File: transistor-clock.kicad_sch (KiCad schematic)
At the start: 48 parts, among them J1 Screw_Terminal_01x02, J10 m0_return, J11 m1_return, J12 h0_return, J13 h1_return, J8 s0_return, J9 s1_return, Q1 MMBT3904, Q2 MMBT3904, Q3 DMP3099L, Q4 2N7002, Q5 MMBT3904, Q6 MMBT3904, Q7 MMBT3904, Q8 MMBT3904, T1 Transformer_1P_SS, T2 CL2-20-12

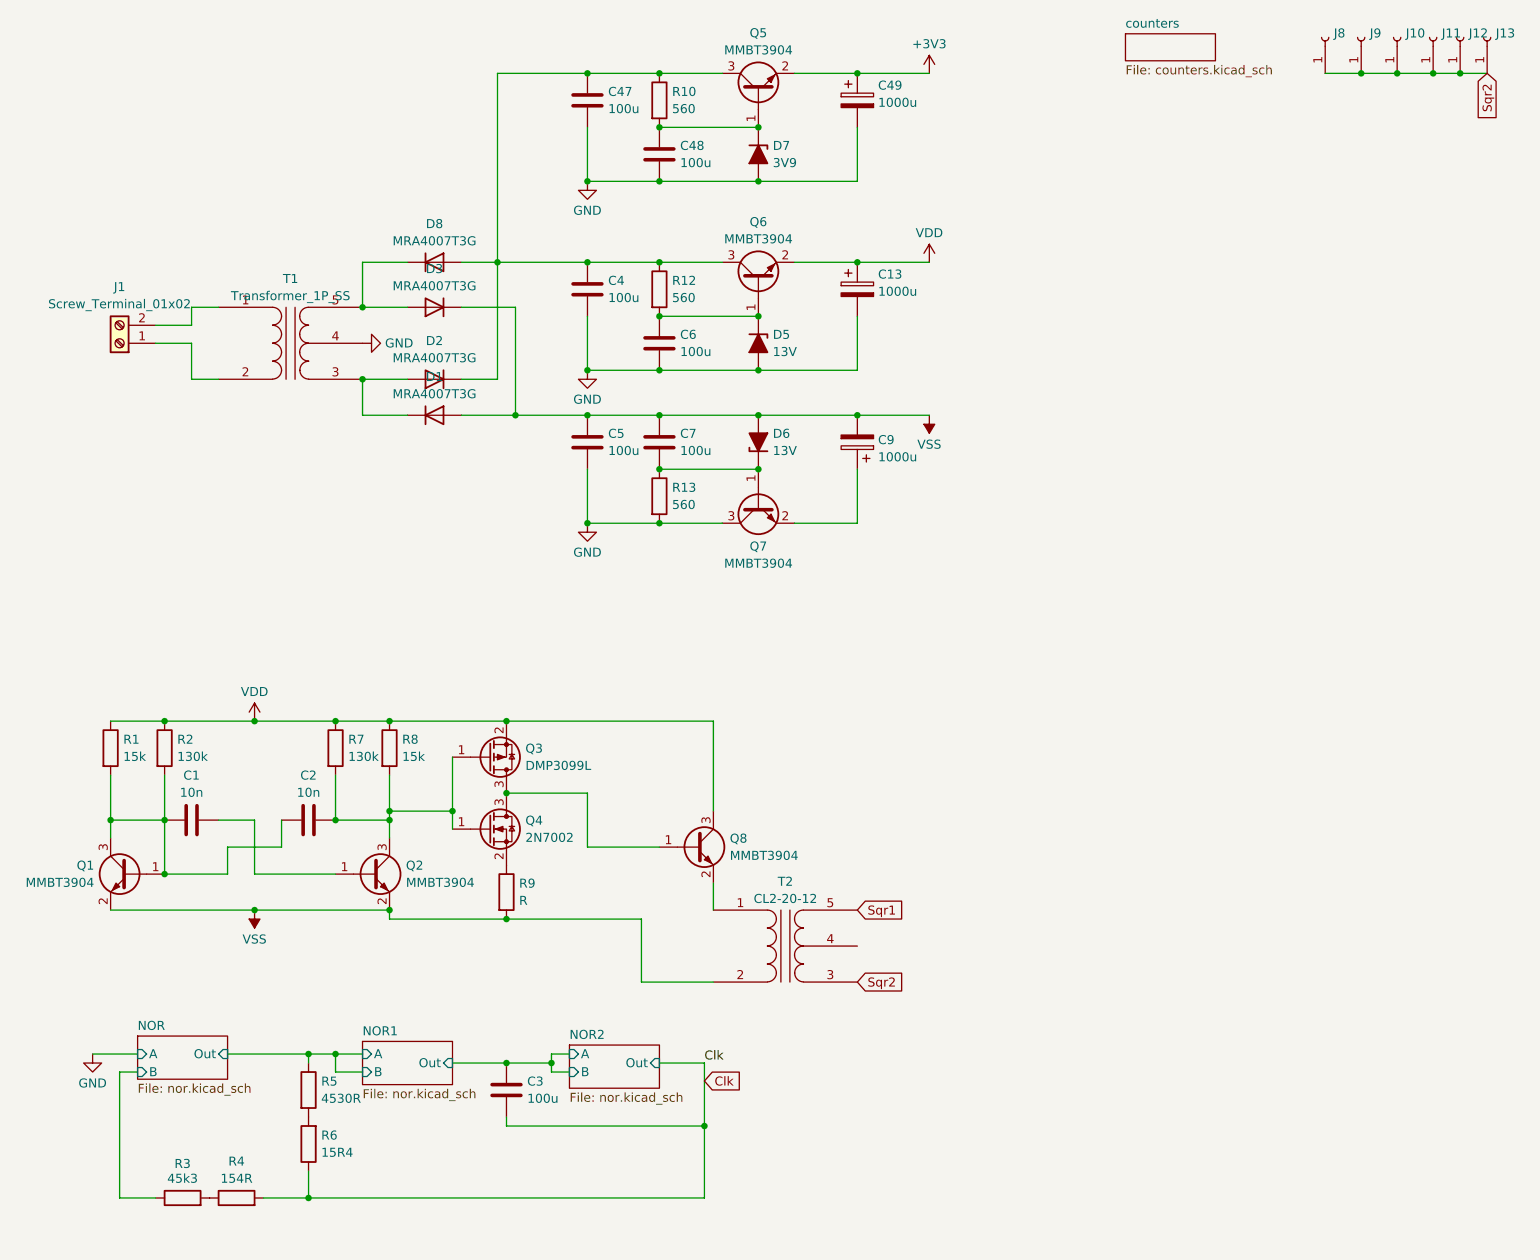
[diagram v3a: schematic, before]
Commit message: corrected output/input type of pins
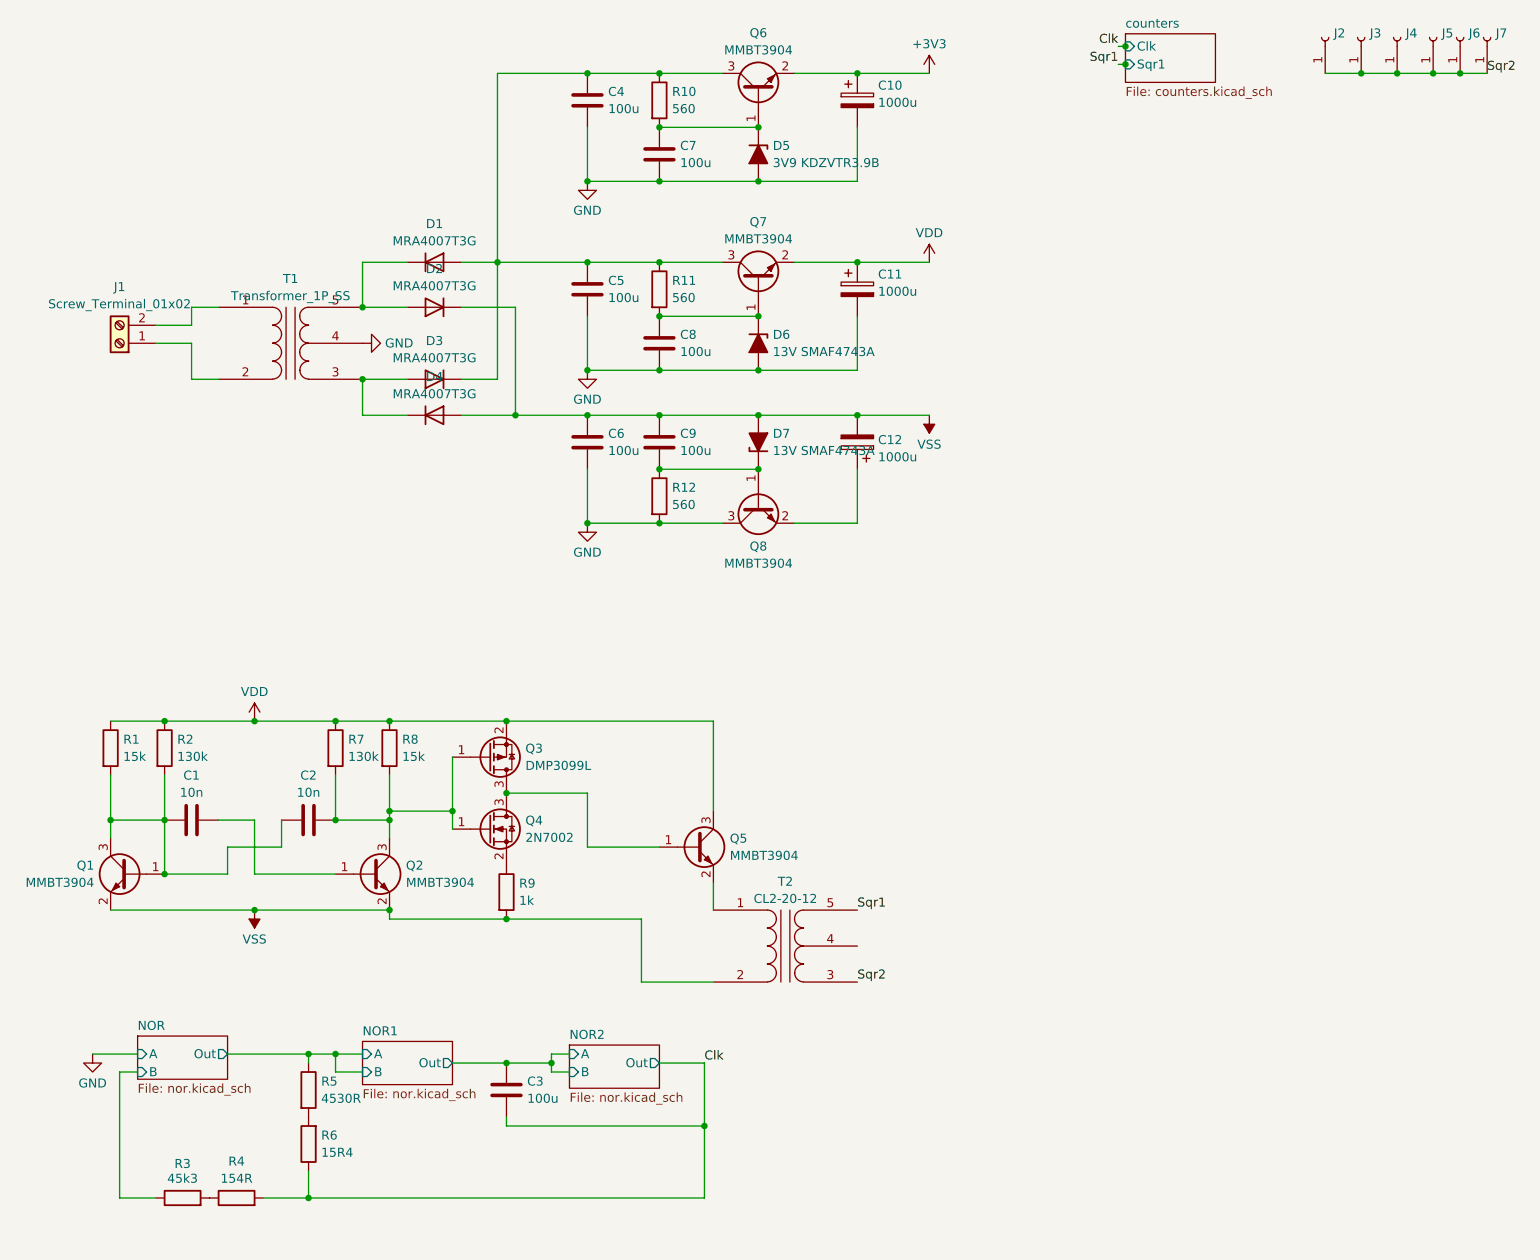
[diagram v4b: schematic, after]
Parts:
- C1, C2, C3: footprint (none) -> Capacitor_SMD:C_0603_1608Metric
- C10: renamed from C49; footprint (none) -> Capacitor_SMD:CP_Elec_5x3
- C11: renamed from C13; footprint (none) -> Capacitor_SMD:CP_Elec_5x3
- C12: renamed from C9; footprint (none) -> Capacitor_SMD:CP_Elec_5x3
- C4: renamed from C47; footprint (none) -> Capacitor_SMD:C_0603_1608Metric
- C5: renamed from C4; footprint (none) -> Capacitor_SMD:C_0603_1608Metric
- C6: renamed from C5; footprint (none) -> Capacitor_SMD:C_0603_1608Metric
- C7: renamed from C48; footprint (none) -> Capacitor_SMD:C_0603_1608Metric
- C8: renamed from C6; footprint (none) -> Capacitor_SMD:C_0603_1608Metric
- C9: renamed from C7; footprint (none) -> Capacitor_SMD:C_0603_1608Metric
- D5: renamed from D7; value 3V9 -> 3V9 KDZVTR3.9B; footprint (none) -> Diode_SMD:D_SOD-123
- D6: renamed from D5; value 13V -> 13V SMAF4743A; footprint (none) -> Diode_SMD:Vishay_SMPA
- D7: renamed from D6; value 13V -> 13V SMAF4743A; footprint (none) -> Diode_SMD:Vishay_SMPA
- J1: footprint (none) -> TerminalBlock:TerminalBlock_MaiXu_MX126-5.0-02P_1x02_P5.00mm
- J2: renamed from J8; value s0_return -> Conn_01x01_Socket; footprint (none) -> Connector_PinHeader_2.54mm:PinHeader_1x01_P2.54mm_Vertical
- J3: renamed from J9; value s1_return -> Conn_01x01_Socket; footprint (none) -> Connector_PinHeader_2.54mm:PinHeader_1x01_P2.54mm_Vertical
- J4: renamed from J10; value m0_return -> Conn_01x01_Socket; footprint (none) -> Connector_PinHeader_2.54mm:PinHeader_1x01_P2.54mm_Vertical
- J5: renamed from J11; value m1_return -> Conn_01x01_Socket; footprint (none) -> Connector_PinHeader_2.54mm:PinHeader_1x01_P2.54mm_Vertical
- J6: renamed from J12; value h0_return -> Conn_01x01_Socket; footprint (none) -> Connector_PinHeader_2.54mm:PinHeader_1x01_P2.54mm_Vertical
- J7: renamed from J13; value h1_return -> Conn_01x01_Socket; footprint (none) -> Connector_PinHeader_2.54mm:PinHeader_1x01_P2.54mm_Vertical
- R9: value R -> 1k; footprint (none) -> Resistor_SMD:R_0402_1005Metric
- renumbered D8 to D1, D3 to D2, D2 to D3, D1 to D4, Q8 to Q5, Q5 to Q6, Q6 to Q7, Q7 to Q8, R12 to R11, R13 to R12
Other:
- sheet counters ports: added Clk, Sqr1; removed none

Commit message: replace bcd logic with bin-to-dec module
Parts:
- removed C3: 100u, Capacitor_SMD:C_0603_1608Metric, symbol Device:C
- added C2: 100u, Capacitor_SMD:C_0603_1608Metric, symbol Device:C
- added U1: ~, symbol custom:BDC_nands
- renumbered C2 to C3, R4 to R1, R12 to R10, R5 to R11, R6 to R12, R3 to R2, R1 to R3, R2 to R4, R7 to R5, R8 to R6, R9 to R7, R10 to R8, R11 to R9
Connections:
- net NOR/Out is gone; now on net Clk: R11.1
- net Clk: now also U1.48; no longer R1.2, R12.1
- net NOR/B: no longer names the net of R2.1
- net NOR/B: now also R12.1, C2.1
- new net: U1.18, U1.49, U1.50
- new net: C2.2, U1.15, U1.20, U1.22
- new net: R1.2, U1.11, U1.13
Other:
- removed sheet NOR
- removed sheet NOR1
- removed sheet NOR2
- moved on the sheet: R1, R11, R12, R2
